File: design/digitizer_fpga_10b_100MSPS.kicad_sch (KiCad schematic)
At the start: 4 parts

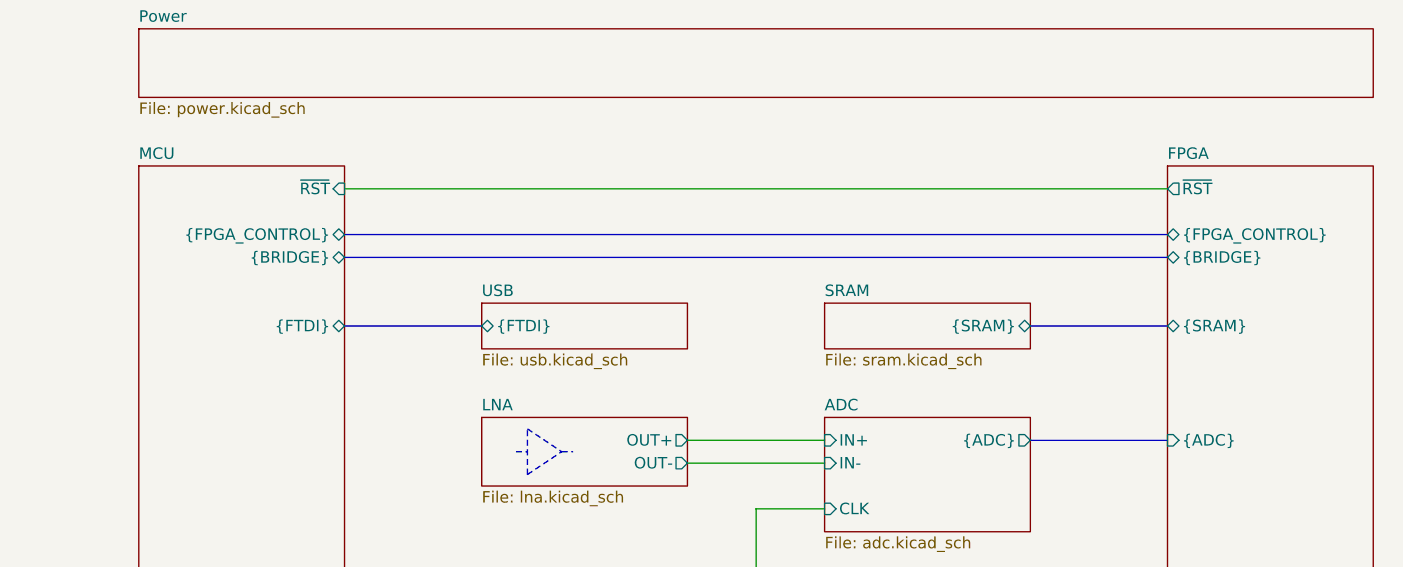
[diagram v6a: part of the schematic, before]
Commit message: Added FTDI RST support
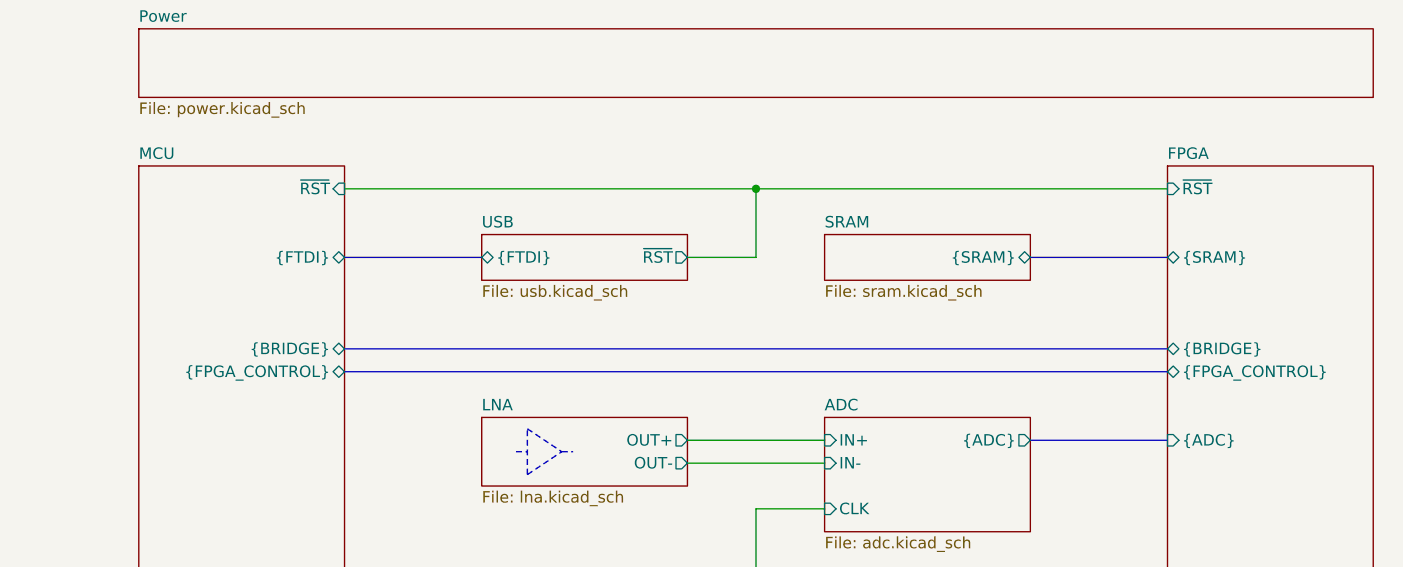
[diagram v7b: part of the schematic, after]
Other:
- sheet USB ports: added ~RST; removed none
